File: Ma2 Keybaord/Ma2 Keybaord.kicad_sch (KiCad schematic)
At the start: 98 parts, among them J1 Conn_01x05, J2 Conn_01x02, J3 USB_C_Receptacle_USB2.0, J4 Conn_01x02, J5 Conn_01x03, SW1 MX_SW_HS, SW10 MX_SW_HS, SW11 MX_SW_HS, SW12 MX_SW_HS, SW13 MX_SW_HS, SW14 MX_SW_HS, SW15 MX_SW_HS, SW16 MX_SW_HS, SW17 MX_SW_HS, SW18 MX_SW_HS, SW19 MX_SW_HS, SW2 MX_SW_HS, SW20 MX_SW_HS, SW21 MX_SW_HS, SW22 MX_SW_HS, SW23 MX_SW_HS, SW24 MX_SW_HS, SW25 MX_SW_HS, SW26 MX_SW_HS, SW27 MX_SW_HS, SW28 MX_SW_HS, SW29 MX_SW_HS, SW3 MX_SW_HS, SW30 MX_SW_HS, SW31 MX_SW_HS, SW32 MX_SW_HS, SW33 MX_SW_HS, SW34 MX_SW_HS, SW35 MX_SW_HS, SW36 MX_SW_HS, SW37 MX_SW_HS, SW38 MX_SW_HS, SW39 MX_SW_HS, SW4 MX_SW_HS, SW40 MX_SW_HS, SW41 MX_SW_HS, SW42 MX_SW_HS, SW43 MX_SW_HS, SW44 MX_SW_HS, SW45 MX_SW_HS, SW46 MX_SW_HS, SW47 MX_SW_HS, SW48 MX_SW_HS, SW49 MX_SW_HS, SW5 MX_SW_HS, SW50 MX_SW_HS, SW51 MX_SW_HS, SW52 MX_SW_HS, SW53 MX_SW_HS, SW54 MX_SW_HS, SW55 MX_SW_HS, SW56 MX_SW_HS, SW57 MX_SW_HS, SW58 MX_SW_HS, SW59 MX_SW_HS, SW6 MX_SW_HS, SW60 MX_SW_HS, SW61 MX_SW_HS, SW62 MX_SW_HS, SW63 MX_SW_HS, SW64 MX_SW_HS, SW65 MX_SW_HS, SW66 MX_SW_HS, SW67 MX_SW_HS, SW68 MX_SW_HS, SW69 MX_SW_HS, SW7 MX_SW_HS, SW70 MX_SW_HS, SW71 MX_SW_HS, SW72 MX_SW_HS, SW73 MX_SW_HS, SW74 MX_SW_HS, SW75 MX_SW_HS, SW76 MX_SW_HS, SW77 MX_SW_HS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

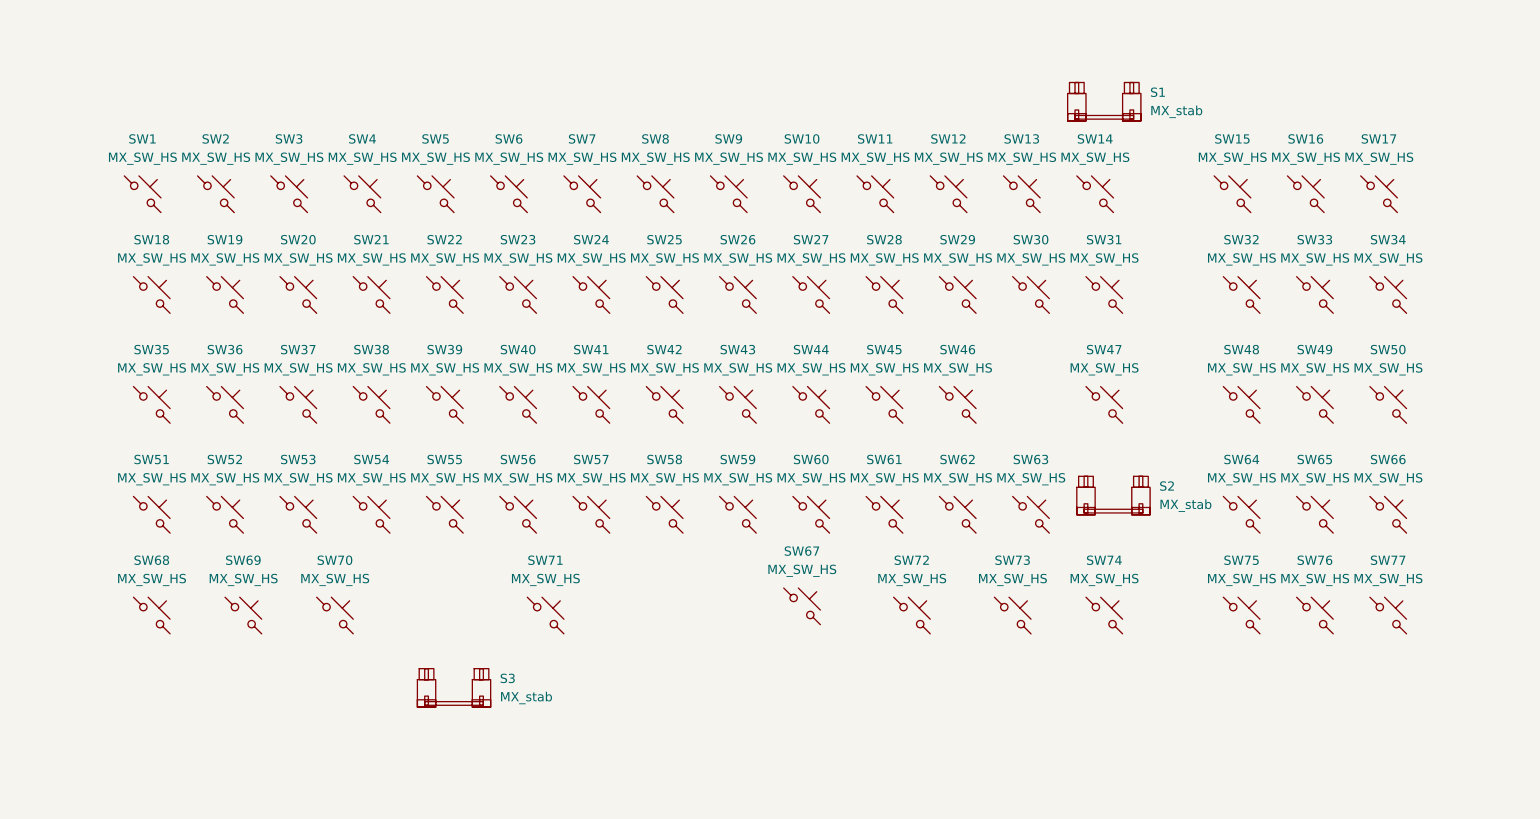
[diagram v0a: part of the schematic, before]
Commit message: more work on the keyboard lay out on the PCB also making 4.5U stab
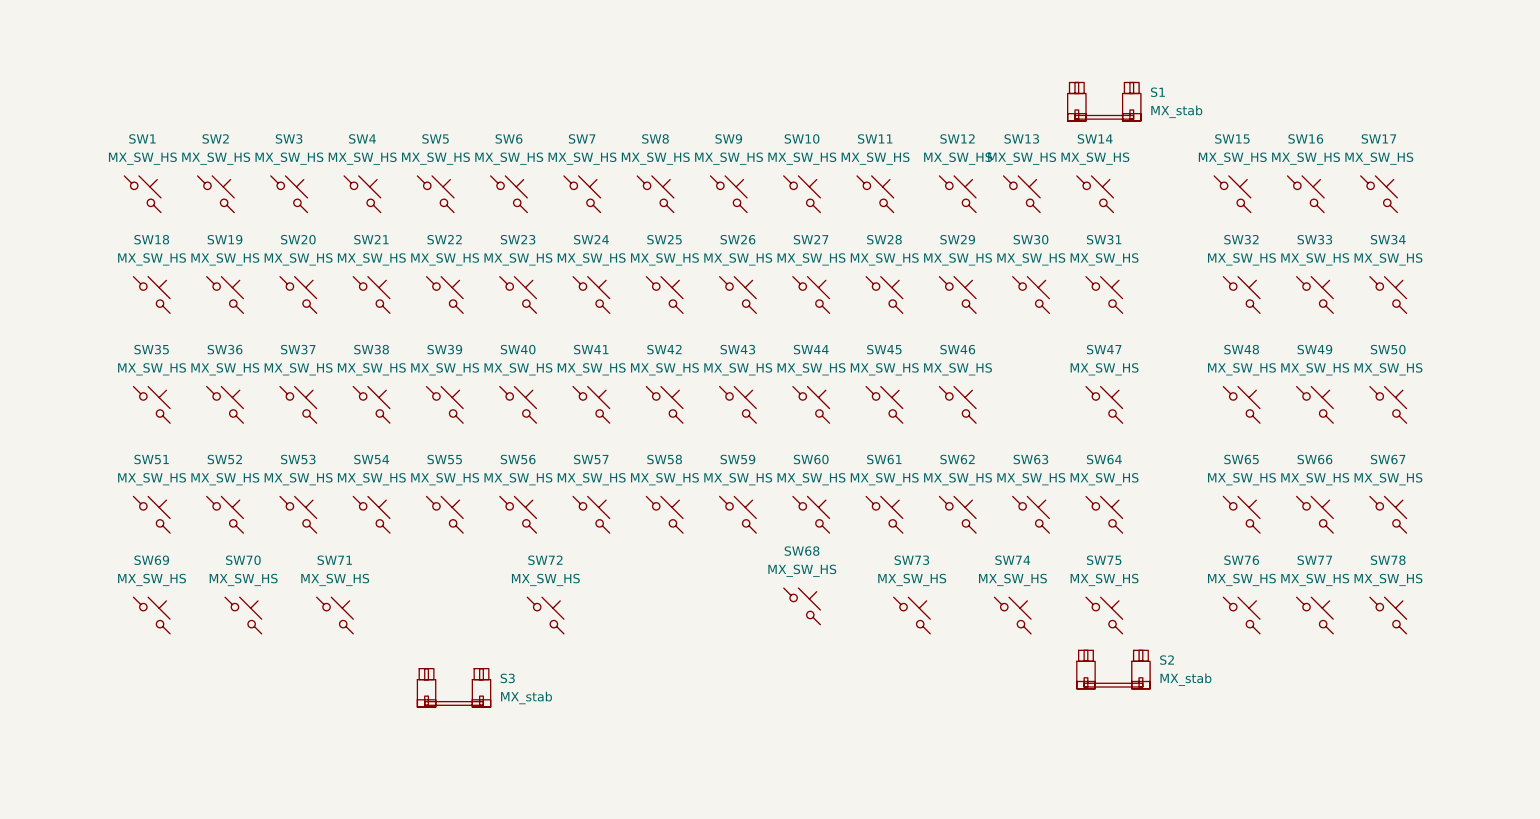
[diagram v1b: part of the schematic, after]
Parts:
- added SW64: MX_SW_HS, marbastlib-mx:SW_MX_HS_1u, symbol marbastlib-mx:MX_SW_HS
- SW31: footprint marbastlib-mx:SW_MX_HS_1u -> marbastlib-mx:SW_MX_HS_1.5u
- SW35: footprint marbastlib-mx:SW_MX_HS_1u -> marbastlib-mx:SW_MX_HS_1.75u_stp
- renumbered SW64 to SW65, SW65 to SW66, SW66 to SW67, SW67 to SW68, SW68 to SW69, SW69 to SW70, SW70 to SW71, SW71 to SW72, SW72 to SW73, SW73 to SW74, SW74 to SW75, SW75 to SW76, SW76 to SW77, SW77 to SW78
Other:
- moved on the sheet: S2, SW12
